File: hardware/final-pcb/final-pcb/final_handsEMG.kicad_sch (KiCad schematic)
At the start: 192 parts, among them J1 Conn_02x13_Odd_Even, U1 ADS1299CPAG, U2 STM32L496ZGT6, U3 FT231XQ-R, U6 TPS60403DBVT, U8 TPS72325DBVT, U9 TPS73225DBVT

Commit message: Changed flow of ADS power to easily flow from the Power portion
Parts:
- L1, L2, L4, L5: footprint MLZ2012A3R3W:INDC2012X87N -> (none)
- L3: renamed from dL2; footprint MPZ1005S300C:IND_1005_TDK -> (none)
- U2: footprint STM32L496ZGT6:LQFP144-20x20mm_STM -> STM32L496ZGT6:QFP50P2200X2200X160-144N
- U6: footprint TPS60403DBVT:SOT95P280X145-5N -> SOT95P280X145-5N; Arrow Part Number (none) -> TPS60403DBVT; Arrow Price/Stock (none) -> https://www.arrow.com/en/products/tps60403dbvt/texas-instru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; Height (none) -> 1.45; Manufacturer_Name (none) -> Texas Instruments; Manufacturer_Part_Number (none) -> TPS60403DBVT; Mouser Part Number (none) -> 595-TPS60403DBVT; Mouser Price/Stock (none) -> https://www.mouser.co.uk/ProductDetail/Texas-Instruments/TP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
- U9: footprint TPS73225DBVT:SOT95P280X145-5N -> SOT95P280X145-5N; Arrow Part Number (none) -> TPS73225DBVT; Arrow Price/Stock (none) -> https://www.arrow.com/en/products/tps73225dbvt/texas-instru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; Height (none) -> 1.45; Manufacturer_Name (none) -> Texas Instruments; Manufacturer_Part_Number (none) -> TPS73225DBVT; Mouser Part Number (none) -> 595-TPS73225DBVT; Mouser Price/Stock (none) -> https://www.mouser.co.uk/ProductDetail/Texas-Instruments/TP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
- pC1, pC11, pC4, pC5, pC8, pC9: footprint 03PowerFOOTPRINTS:C1005X5R0J105M -> (none)
- pC10: footprint 03PowerFOOTPRINTS:C1608X5R0J225M -> (none)
- pC12: value 10uF -> 100uF; footprint 03PowerFOOTPRINTS:C1608X5R0J106M -> (none)
- pC13: footprint 03PowerFOOTPRINTS:GRM31CR60J107ME39L -> (none)
- pC14: footprint 03PowerFOOTPRINTS:LMK316BJ476ML-T -> (none)
- pC15, pC20, pC22, pC24: footprint 03PowerFOOTPRINTS:04025A100KAT -> (none)
- pC16, pC26, pC27, pC28, pC29: footprint 03PowerFOOTPRINTS:C1005X5R1C104K -> (none)
- pC17: footprint 03PowerFOOTPRINTS:04025A331KAT -> (none)
- pC18: footprint 03PowerFOOTPRINTS:04025A330KAT -> (none)
- pC19, pC6, pC7: footprint 03PowerFOOTPRINTS:JMK212BJ226MG-T -> (none)
- pC2: footprint 03PowerFOOTPRINTS:GRM21BR61A106KE19 -> (none)
- pC21, pC23: footprint 03PowerFOOTPRINTS:C1608X5R0J106M -> (none)
- pC3: footprint 03PowerFOOTPRINTS:GRM21BR61A106KE19L -> (none)
- pD2: footprint SMD-LED-CLEAR-GREEN_0603_:LED-0603 -> (none)
- pD3: footprint LED-SMD-RED-DIFFUSED_0603_:LED-0603 -> (none)
- pJP2, pJP3, pJP4, pJP5, pJP6, pJP7, pJP8: footprint 03PowerFOOTPRINTS:SAMTEC-TMM-103-02-X-S -> (none)
- pL1: footprint 03PowerFOOTPRINTS:LPS4018-332MLC -> (none)
- pL2, pL3: footprint 03PowerFOOTPRINTS:LPS4018-222MLC -> (none)
- pL4, pL5: footprint 03PowerFOOTPRINTS:IND_3010_TDK -> (none)
- pQ1: footprint 03PowerFOOTPRINTS:SI2333DS -> (none)
- pR10, pR12, pR4: footprint 03PowerFOOTPRINTS:CRCW04020000Z0EDC -> (none)
- pR13, pR18, pR23, pR26: footprint 03PowerFOOTPRINTS:CRCW040220R0FKED -> (none)
- pR14: footprint 03PowerFOOTPRINTS:CRCW040288K7FKED -> (none)
- pR15: footprint 03PowerFOOTPRINTS:CRCW040216K9FKED -> (none)
- pR16: footprint 03PowerFOOTPRINTS:CRCW04023K01FKED -> (none)
- pR17: footprint 03PowerFOOTPRINTS:CRCW04022K00FKED -> (none)
- pR19: footprint 03PowerFOOTPRINTS:CRCW040215K0FKED -> (none)
- pR2, pR29, pR30, pR31: footprint 03PowerFOOTPRINTS:CRCW04021R00JNED -> (none)
- pR20: footprint 03PowerFOOTPRINTS:CRCW0402324KFKED -> (none)
- pR21: footprint 03PowerFOOTPRINTS:CRCW0402121KFKED -> (none)
- pR22: footprint 03PowerFOOTPRINTS:CRCW0402105KFKED -> (none)
- pR24: footprint 03PowerFOOTPRINTS:CRCW0402806KFKED -> (none)
- pR25: footprint 03PowerFOOTPRINTS:CRCW0402649KFKED -> (none)
- pR27: footprint 03PowerFOOTPRINTS:CRCW0402232KFKED -> (none)
- pR28: footprint 03PowerFOOTPRINTS:CRCW0402464KFKED -> (none)
- pR3, pR9: footprint 03PowerFOOTPRINTS:CRCW0402100KFKED -> (none)
- pR32, pR33, pR34, pR35, pR5, pR7: footprint 03PowerFOOTPRINTS:CRCW04021K00JNED -> (none)
- pR6, pR8: footprint 03PowerFOOTPRINTS:CRCW04022K20FKED -> (none)
- pU1: footprint 03PowerFOOTPRINTS:LTC3586EUFE -> (none)
- sC42: footprint TAJA475K016R:CAPMP3216X166 -> (none)
- sJ2: footprint S2B-PH-K-S:CONN_S2B-PH-K-S_JST -> (none)
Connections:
- net +5V: no longer C46.1, C47.1, C58.1, L1.2, U6.2 (IN), U9.1 (IN), U9.3 (EN)
- net AVBUS: no longer sR54.2
- net USB_VBUS: now also sR54.2
- net -5V renamed -5VCC
- new net 5VCC: C46.1, C47.1, C58.1, L1.2, U6.2 (IN), U9.1 (IN), U9.3 (EN)

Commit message: organized schematic, needs verification (4.6.25)
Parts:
- L1, L2, L4, L5: footprint (none) -> MLZ2012A3R3W:INDC2012X87N
- U2: footprint STM32L496ZGT6:QFP50P2200X2200X160-144N -> STM32L496ZGT6:LQFP144-20x20mm_STM
- U3: renamed from pU1; footprint (none) -> 03PowerFOOTPRINTS:LTC3586EUFE
- U6: footprint SOT95P280X145-5N -> TPS60403DBVT:SOT95P280X145-5N; Arrow Part Number TPS60403DBVT -> (none); Arrow Price/Stock https://www.arrow.com/en/products/tps60403dbvt/texas-instru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 -> (none); Height 1.45 -> (none); Manufacturer_Name Texas Instruments -> (none); Manufacturer_Part_Number TPS60403DBVT -> (none); Mouser Part Number 595-TPS60403DBVT -> (none); Mouser Price/Stock https://www.mouser.co.uk/ProductDetail/Texas-Instruments/TP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 -> (none)
- U9: footprint SOT95P280X145-5N -> TPS73225DBVT:SOT95P280X145-5N; Arrow Part Number TPS73225DBVT -> (none); Arrow Price/Stock https://www.arrow.com/en/products/tps73225dbvt/texas-instru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 -> (none); Height 1.45 -> (none); Manufacturer_Name Texas Instruments -> (none); Manufacturer_Part_Number TPS73225DBVT -> (none); Mouser Part Number 595-TPS73225DBVT -> (none); Mouser Price/Stock https://www.mouser.co.uk/ProductDetail/Texas-Instruments/TP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 -> (none)
- dL2: renamed from L3; footprint (none) -> MPZ1005S300C:IND_1005_TDK
- pC1, pC11, pC4, pC5, pC8, pC9: footprint (none) -> 03PowerFOOTPRINTS:C1005X5R0J105M
- pC10: footprint (none) -> 03PowerFOOTPRINTS:C1608X5R0J225M
- pC12: value 100uF -> 10uF; footprint (none) -> 03PowerFOOTPRINTS:C1608X5R0J106M
- pC13: footprint (none) -> 03PowerFOOTPRINTS:GRM31CR60J107ME39L
- pC14: footprint (none) -> 03PowerFOOTPRINTS:LMK316BJ476ML-T
- pC15, pC20, pC22, pC24: footprint (none) -> 03PowerFOOTPRINTS:04025A100KAT
- pC16, pC26, pC27, pC28, pC29: footprint (none) -> 03PowerFOOTPRINTS:C1005X5R1C104K
- pC17: footprint (none) -> 03PowerFOOTPRINTS:04025A331KAT
- pC18: footprint (none) -> 03PowerFOOTPRINTS:04025A330KAT
- pC19, pC6, pC7: footprint (none) -> 03PowerFOOTPRINTS:JMK212BJ226MG-T
- pC2: footprint (none) -> 03PowerFOOTPRINTS:GRM21BR61A106KE19
- pC21, pC23: footprint (none) -> 03PowerFOOTPRINTS:C1608X5R0J106M
- pC3: footprint (none) -> 03PowerFOOTPRINTS:GRM21BR61A106KE19L
- pD2: footprint (none) -> SMD-LED-CLEAR-GREEN_0603_:LED-0603
- pD3: footprint (none) -> LED-SMD-RED-DIFFUSED_0603_:LED-0603
- pJP2, pJP3, pJP4, pJP5, pJP6, pJP7, pJP8: footprint (none) -> 03PowerFOOTPRINTS:SAMTEC-TMM-103-02-X-S
- pL1: footprint (none) -> 03PowerFOOTPRINTS:LPS4018-332MLC
- pL2, pL3: footprint (none) -> 03PowerFOOTPRINTS:LPS4018-222MLC
- pL4, pL5: footprint (none) -> 03PowerFOOTPRINTS:IND_3010_TDK
- pQ1: footprint (none) -> 03PowerFOOTPRINTS:SI2333DS
- pR10, pR12, pR4: footprint (none) -> 03PowerFOOTPRINTS:CRCW04020000Z0EDC
- pR13, pR18, pR23, pR26: footprint (none) -> 03PowerFOOTPRINTS:CRCW040220R0FKED
- pR14: footprint (none) -> 03PowerFOOTPRINTS:CRCW040288K7FKED
- pR15: footprint (none) -> 03PowerFOOTPRINTS:CRCW040216K9FKED
- pR16: footprint (none) -> 03PowerFOOTPRINTS:CRCW04023K01FKED
- pR17: footprint (none) -> 03PowerFOOTPRINTS:CRCW04022K00FKED
- pR19: footprint (none) -> 03PowerFOOTPRINTS:CRCW040215K0FKED
- pR2, pR29, pR30, pR31: footprint (none) -> 03PowerFOOTPRINTS:CRCW04021R00JNED
- pR20: footprint (none) -> 03PowerFOOTPRINTS:CRCW0402324KFKED
- pR21: footprint (none) -> 03PowerFOOTPRINTS:CRCW0402121KFKED
- pR22: footprint (none) -> 03PowerFOOTPRINTS:CRCW0402105KFKED
- pR24: footprint (none) -> 03PowerFOOTPRINTS:CRCW0402806KFKED
- pR25: footprint (none) -> 03PowerFOOTPRINTS:CRCW0402649KFKED
- pR27: footprint (none) -> 03PowerFOOTPRINTS:CRCW0402232KFKED
- pR28: footprint (none) -> 03PowerFOOTPRINTS:CRCW0402464KFKED
- pR3, pR9: footprint (none) -> 03PowerFOOTPRINTS:CRCW0402100KFKED
- pR32, pR33, pR34, pR35, pR5, pR7: footprint (none) -> 03PowerFOOTPRINTS:CRCW04021K00JNED
- pR6, pR8: footprint (none) -> 03PowerFOOTPRINTS:CRCW04022K20FKED
- sC42: footprint (none) -> TAJA475K016R:CAPMP3216X166
- sJ2: footprint (none) -> S2B-PH-K-S:CONN_S2B-PH-K-S_JST
- renumbered U3 to U4
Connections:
- net 5VCC is gone; now on net +5V: C46.1, C47.1, C58.1, L1.2, U6.2 (IN), U9.1 (IN), U9.3 (EN)
- net PA6 is gone; now on net DOUT: U2.42 (PA6)
- net PA7 is gone; now on net DIN: U2.43 (PA7)
- net RXD is gone; now on net PD5: dR6.1
- net SCLK is gone; now on net PA1: U1.40 (SCLK)
- net START is gone; now on net PB0: U1.38 (START)
- net TXD is gone; now on net PD6: dR7.1
- net /CS is gone; now on net PA4: U1.39 (~{CS})
- net /DRDY is gone; now on net PA5: U1.47 (~{DRDY})
- net /PWDN is gone; now on net PC4: U1.35 (~{PWDN})
- net /RESET is gone; now on net PC5: U1.36 (~{RESET})
- net *FAULT: now also U2.114 (PD0)
- net +3V3: now also U4.12 (VCC), U4.20 (VCCIO)
- net 3V3OUT: no longer U4.20 (VCCIO)
- net AVBUS: now also sR54.2; no longer U4.12 (VCC)
- net EN1: now also U2.115 (PD1)
- net EN2: now also U2.116 (PD2)
- net EN3: now also U2.117 (PD3)
- net EN4: now also U2.118 (PD4)
- net ILIM0: now also U2.113 (PC12)
- net ILIM1: now also U2.112 (PC11)
- net MODE: now also U2.111 (PC10)
- net USB_VBUS: no longer sR54.2
- net PD5: now reaches U2.119 (PD5)
- net PD6: now reaches U2.122 (PD6)
- net PA5: now reaches U2.41 (PA5)
- net PC4: now reaches U2.44 (PC4)
- net PC5: now reaches U2.45 (PC5)
- net PB0: now reaches U2.46 (PB0)
- net -5VCC renamed -5V
- net DTR#: no longer names the net of U4.18 (DTR#)
- no-connect marks 104 -> 91
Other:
- note added: "ADS1299"
- note added: "FT231XQ-R"
- note added: "LTC3586"
- note added: "STM32L496ZGT6"
- moved on the sheet: C1, C11, C12, C13, C14, C15, C17, C18, C19, C2, C21, C22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

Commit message: fixed and organized schematic (4.6.25)
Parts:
- removed pC26, pC27: 0.1uF, 03PowerFOOTPRINTS:C1005X5R1C104K, symbol Device:C_Small
- removed pJP2, pJP3, pJP4, pJP5, pJP6, pJP7, pJP8: TMM-103-02-L-S, 03PowerFOOTPRINTS:SAMTEC-TMM-103-02-X-S, symbol TMM-103-02-L-S:TMM-103-02-L-S
- removed pR32, pR33: 1K, 03PowerFOOTPRINTS:CRCW04021K00JNED, symbol Device:R_Small
- pR34, pR35: value 1K -> 10K
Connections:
- net EN3: now also pR34.1
- net EN4: now also pR35.1
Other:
- moved on the sheet: pC28, pC29, pR34, pR35

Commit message: finalpcb is not final yet (4.12.25)
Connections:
- net DGND is gone; now on net GND: U1.33 (DGND), U1.49 (DGND), U1.51 (DGND)
- net VBAT is gone; now on net +3V3: U2.6 (VBAT)
- net +2V5: now also sC56.+, sC59.+; no longer sC56.1, sC59.1
- net AVBUS: now also sC42.+; no longer sC42.1
- net GND: now also U2.30 (VSSA/VREF-), U2.31 (VREF-), sC42.-, sC56.-, sC57.2, sC58.2, sC59.-; no longer sC42.2
- net GNDA: no longer U2.30 (VSSA/VREF-), U2.31 (VREF-), sC56.2, sC57.2, sC58.2, sC59.2
- net LDO3V3: now also pD2.+ (A), pD3.+ (A); no longer pD2.2 (A), pD3.2 (A)
- net at sR51.1, sU12.3 (FAULT): now also sLD7.- (K); no longer sLD7.1 (K)
- net at sR45.1: now also sLD7.+ (A); no longer sLD7.2 (A)
- net at pR5.1: now also pD2.- (K); no longer pD2.1 (K)
- net at sT2.3 (C): now also sLD8.- (K); no longer sLD8.1 (K)
- net at sR41.1: now also sLD8.+ (A); no longer sLD8.2 (A)
- net at pR7.1: now also pD3.- (K); no longer pD3.1 (K)

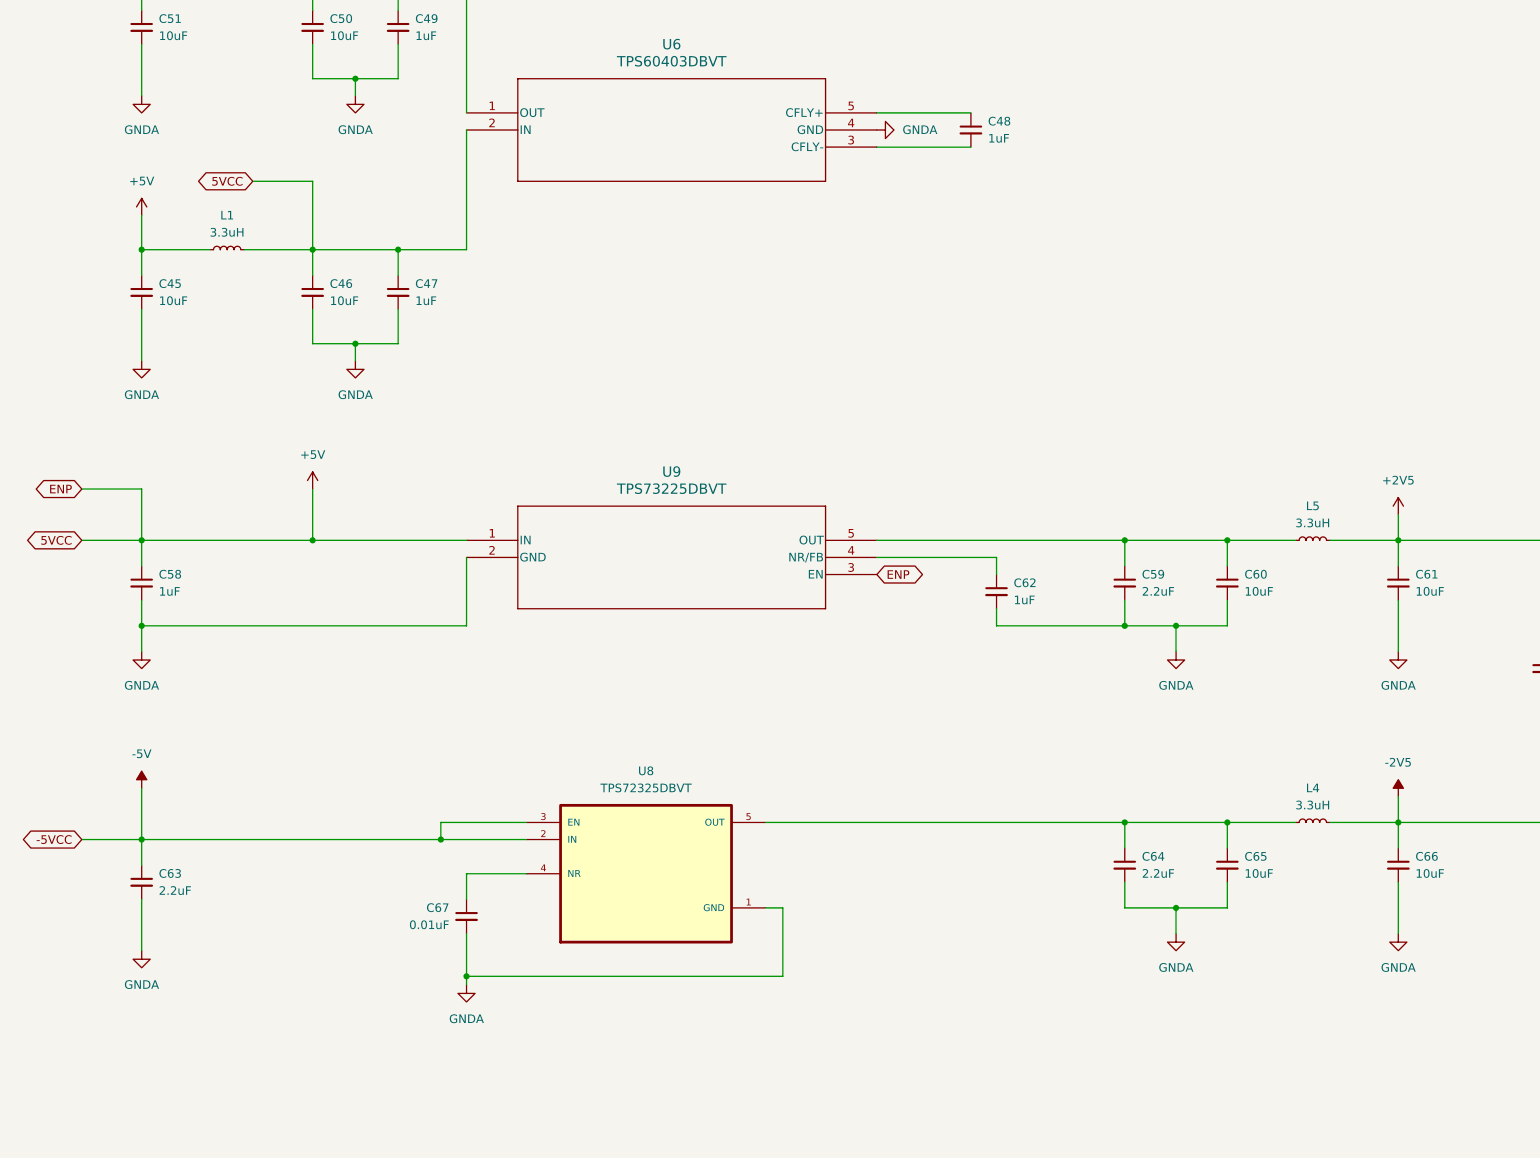
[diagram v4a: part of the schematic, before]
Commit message: traces got fucked up so i rerouted pmic (4.13.25)
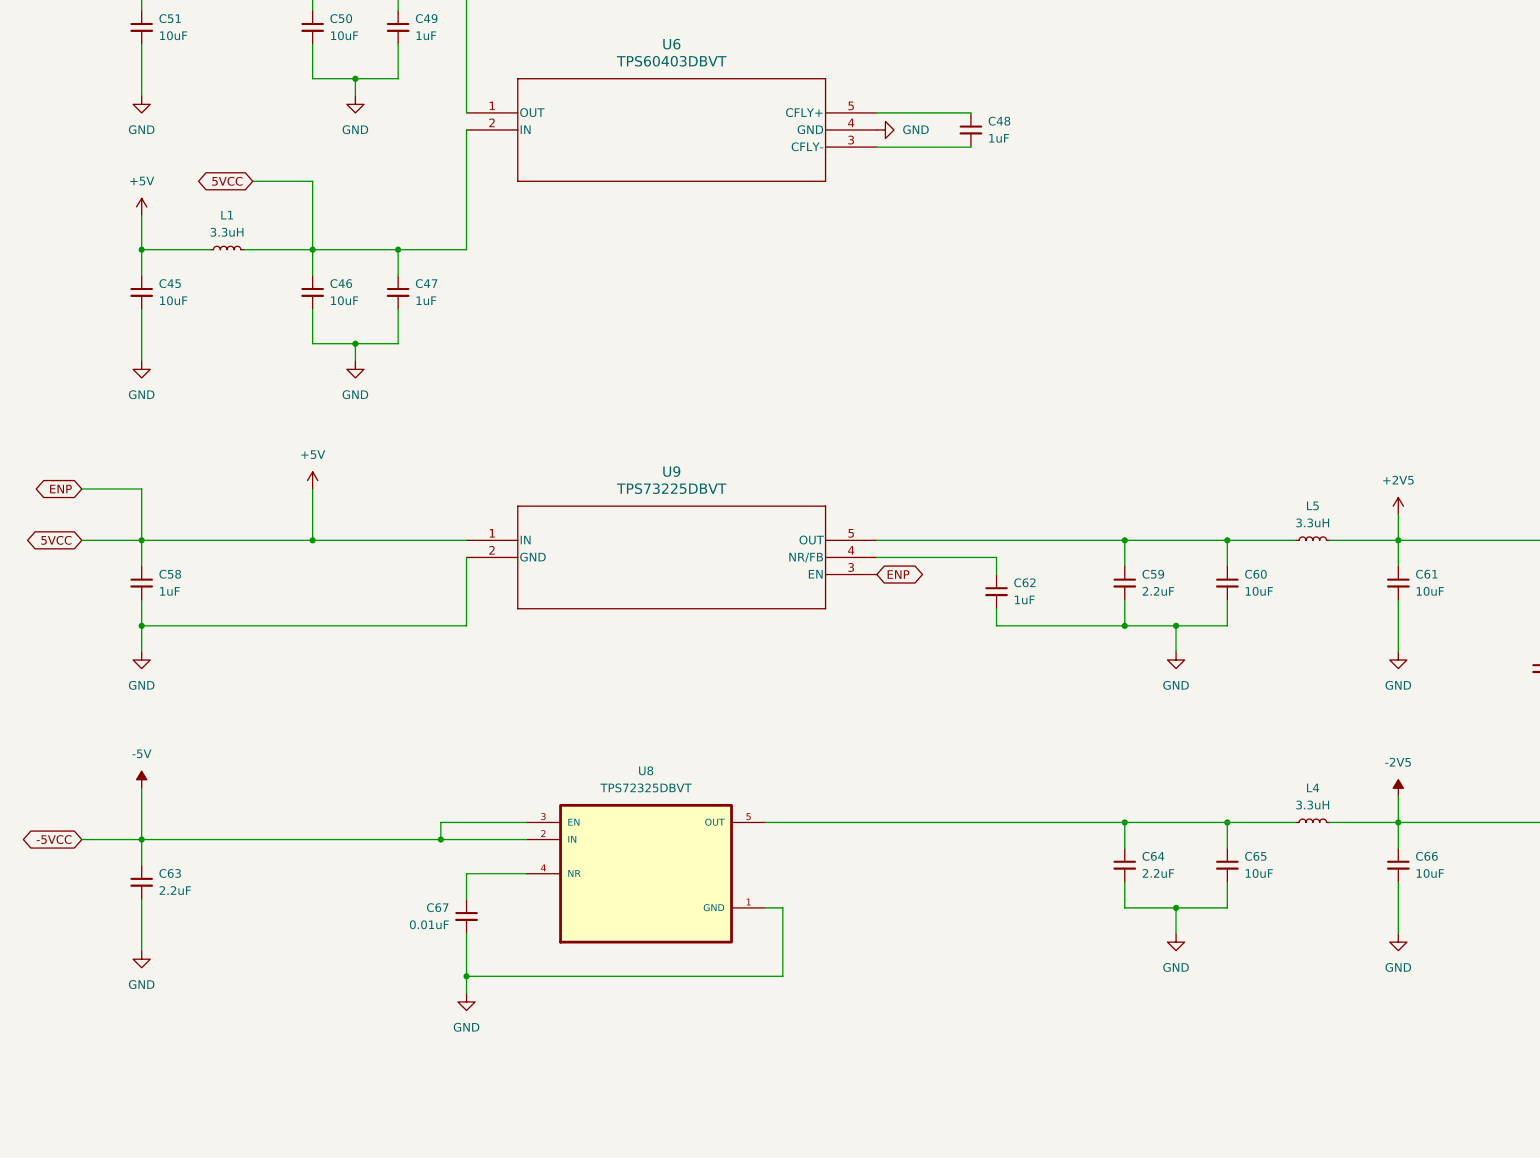
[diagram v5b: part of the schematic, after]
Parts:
- pL4, pL5: footprint 03PowerFOOTPRINTS:IND_3010_TDK -> LPS4018_472MRC:IND_LPS4018-472MRC
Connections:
- net GND: now also C45.2, C46.2, C47.2, C49.2, C50.2, C51.2, C58.2, C59.2, C60.2, C61.2, C62.2, C63.2, C64.2, C65.2, C66.2, C67.2, U6.4 (GND), U8.1 (GND), U9.2 (GND)
- net GNDA: no longer C45.2, C46.2, C47.2, C49.2, C50.2, C51.2, C58.2, C59.2, C60.2, C61.2, C62.2, C63.2, C64.2, C65.2, C66.2, C67.2, U6.4 (GND), U8.1 (GND), U9.2 (GND)

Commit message: basically done, everyone please verify if possible (4.16.25)
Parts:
- added C16: 1nF, CC0402KRX7R7BB102:YAG_CC0402_YAG, symbol Device:C_Small
- added R5: 1M, RC0402JR-071ML:RC0402N_YAG, symbol Device:R_Small
- added TP1: RAW, 5000:KEYSTONE_5000, symbol Connector:TestPoint
- added TP2: LDO3V3, 5000:KEYSTONE_5000, symbol Connector:TestPoint
- added TP4: +3V3, 5000:KEYSTONE_5000, symbol Connector:TestPoint
- added TP5: -5V, 5001:KEYSTONE_5001, symbol Connector:TestPoint
- added TP6: +5V, 5001:KEYSTONE_5001, symbol Connector:TestPoint
- added TP7: +2V5, 5001:KEYSTONE_5001, symbol Connector:TestPoint
- added TP8: -2V5, 5001:KEYSTONE_5001, symbol Connector:TestPoint
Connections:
- net BIASOUT is gone; now on net BIASIN: U1.63 (BIASOUT)
- net +2V5: now also TP7.1
- net +3V3: now also TP4.1
- net +5V: now also TP6.1
- net -2V5: now also TP8.1
- net -5V: now also TP5.1
- net BAT: now also TP1.1
- net BIASIN: now also C16.2, R5.2
- net BIAS_DRV: now also C16.1, R5.1
- net LDO3V3: now also TP2.1
- net SRB1: no longer C3.8, R1.5, U1.17 (SRB1)
- net SRB2: no longer C3.7, R1.6, U1.18 (SRB2)
- new net _SRB1: C3.8, R1.5, U1.17 (SRB1)
- new net _SRB2: C3.7, R1.6, U1.18 (SRB2)

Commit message: lol forgot buttons (4.16.25)
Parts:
- added RESET1, USER1: TS02-66-60-BK-160-LCR-D, FSM6JSMATR:SW_5-1437565-0, symbol TS02-66-60-BK-160-LCR-D:TS02-66-60-BK-160-LCR-D
- added sC40: [N/A], CC0402KRX7R7BB104:YAG_CC0402_YAG, symbol Device:C_Small
- added sC41: 100nF, CC0402KRX7R7BB104:YAG_CC0402_YAG, symbol Device:C_Small
- added sR42: 220K, RC0603FR-07220KL:RESC1607X60N, symbol Device:R_Small
- added sR43: 330, RC0603FR-07330RL:RESC1607X60N, symbol Device:R_Small
- added sR44: 100, RC0603FR-07100RL:RESC1607X60N, symbol Device:R_Small
- renumbered sJ3 to SWD1
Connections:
- net +3V3: now also USER1.2, USER1.3, sR44.1
- net GND: now also RESET1.2, RESET1.3, sC41.2, sR42.1
- net NRST: now also RESET1.1, RESET1.4, sC41.1
- net PC13: now also sR43.1
- new net: USER1.1, USER1.4, sC40.1, sR42.2, sR43.2
- new net: sC40.2, sR44.2
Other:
- moved on the sheet: SWD1, sD10

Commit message: implemented blakes revisions (4.21.25)
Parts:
- removed RESET1, USER1: TS02-66-60-BK-160-LCR-D, FSM6JSMATR:SW_5-1437565-0, symbol TS02-66-60-BK-160-LCR-D:TS02-66-60-BK-160-LCR-D
- added pR80, pR81, pR82, pR83: 10K, 03PowerFOOTPRINTS:CRCW04021K00JNED, symbol Device:R_Small
- added sB1: USER, PTS645SH50SMTR92 LFS:PTS645S_SMTR92_CNK, symbol PTS645SH50SMTR92:PTS645SH50SMTR92LFS
- added sB2: RESET, PTS645SH50SMTR92 LFS:PTS645S_SMTR92_CNK, symbol PTS645SH50SMTR92:PTS645SH50SMTR92LFS
- added sR55: 10K (DNP), RC0603FR-0710KL:RESC1607X60N, symbol Device:R_Small
- U3: footprint 03PowerFOOTPRINTS:LTC3586EUFE -> LTC3586 Fixed:QFN-38_UFE_LIT
- sR54: value 10K -> 10K (DNP)
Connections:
- net *FAULT: now also pR80.2; no longer U2.114 (PD0)
- net +3V3: now also sB1.2, sB1.3
- net GND: now also sB2.2, sB2.3
- net ILIM0: now also pR81.2; no longer U2.113 (PC12)
- net ILIM1: now also pR82.2; no longer U2.112 (PC11)
- net MODE: now also pR83.2; no longer U2.111 (PC10)
- net NRST: now also sB2.1, sB2.4
- net PA10: now also sR55.1; no longer sCN14.4 (ID), sD6.1 (K)
- net at sC40.1, sR42.2, sR43.2: now also sB1.1, sB1.4
- new net PC10: U2.111 (PC10), pR83.1
- new net PC11: U2.112 (PC11), pR82.1
- new net PC12: U2.113 (PC12), pR81.1
- new net PD0: U2.114 (PD0), pR80.1
- new net USB_ID: sCN14.4 (ID), sD6.1 (K), sR55.2
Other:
- moved on the sheet: sC40, sC41, sR42, sR43, sR44, sR54
